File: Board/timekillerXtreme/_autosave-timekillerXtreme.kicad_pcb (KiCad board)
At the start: 2 copper layers, 61.5 x 105.2 mm, 113 parts, among them J1 Battery, J13 CONN_01X03, J16 PE8, J17 PE9, J18 PE10, J19 PD4, J2 USB_OTG, J20 PD1, J21 PD0, J22 PD3, J23 PE11, J24 Pb12, J3 Conn_Bottom_Expansion, J5 Conn_LCD_Board, J6 uSD, J8 TP_AUDIO_R, J9 TP_AUDIO_L, Q1 IRLML6302, Q2 PMBT3904.215, SW1 PWR, SW2 A, SW3 B, SW4 LEFT, SW5 RIGHT, SW6 DOWN, SW7 UP, SW8 RST, U1 MCP73831, U2 FT230XS-R, U3 NCP1529, U4 TLV431, U5 STM32F407VGT6, U6 USBLC6, U7 AOZ1310, U8 USBLC6, U9 USBLC6, Y1 32.768 KHz, Y2 16MHz

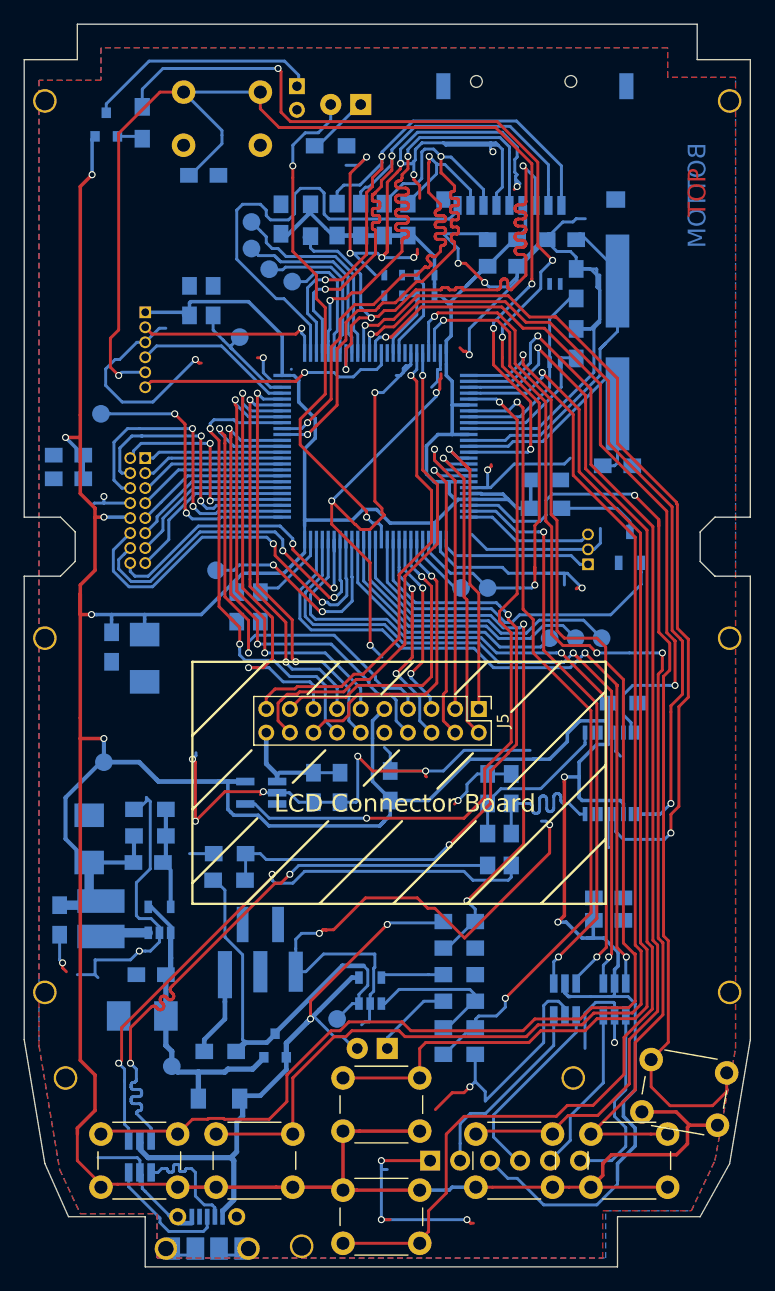
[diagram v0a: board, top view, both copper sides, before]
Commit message: Case and board updated, this will be shipped to the boardhouse and I will call it rev2 if it is ok.
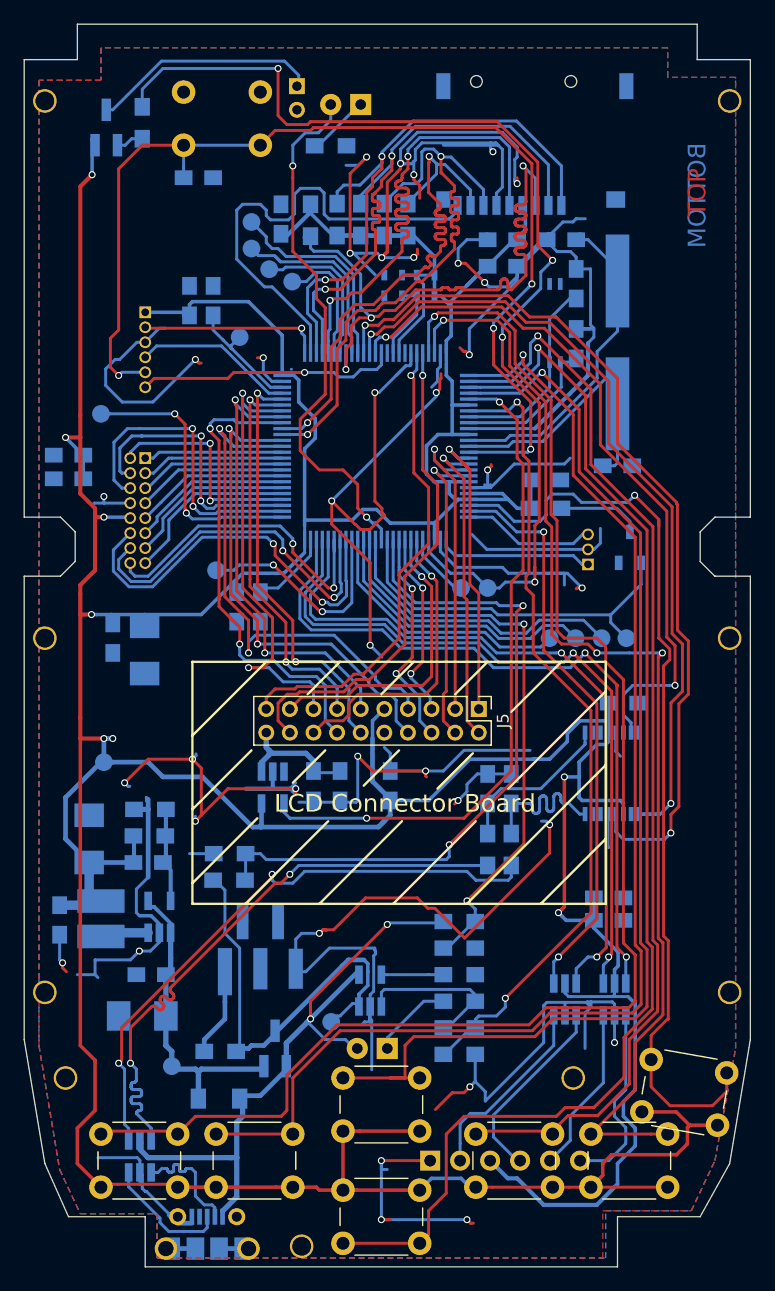
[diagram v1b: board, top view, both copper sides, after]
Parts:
- added VREF: VREF, Measurement_Points:Measurement_Point_Round-SMD-Pad_Small, B.Cu at (168.5, 92.0)
- Q1, Q2: footprint TO_SOT_Packages_SMD:SOT-23 -> TO_SOT_Packages_SMD:SOT-23_Handsoldering
- U1, U3: footprint TO_SOT_Packages_SMD:SOT-23-5 -> TO_SOT_Packages_SMD:SOT-23-5_HandSoldering
- moved SW8 7.91 mm to (137.5, 45.8), turned to 180 degrees
- moved U7 1.07 mm to (138.6, 104.7), turned to 270 degrees
- moved C18 0.76 mm to (125.0, 92.0)
- moved C24 0.70 mm to (127.7, 93.0)
- moved VBATT 0.56 mm to (143.5, 124.5)
- moved C13 0.49 mm to (132.2, 53.0)
- moved U3 0.26 mm to (128.9, 115.6)
- moved J1 0.25 mm to (137.5, 117.8)
- moved Q1 0.25 mm to (138.8, 126.8)
- moved Q2 0.25 mm to (124.5, 48.8)
- moved C32 0.14 mm to (142.0, 104.5)
- moved C33 0.14 mm to (144.2, 104.5)
- moved R8 0.05 mm to (128.1, 108.8)
- renumbered V_USB to VUSB
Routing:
- net RESET: track 105.4 -> 93.7 mm
- net GND: track 475.0 -> 486.5 mm, vias 35 -> 36
- net Net-(C11-Pad1): track 32.2 -> 28.3 mm
- net LCD_BL_SHDN: track 60.3 -> 56.8 mm
- net +3V3: track 503.3 -> 500.2 mm, vias 7 -> 8
- net BTN_1_UP: track 94.3 -> 96.7 mm
- net VBATT_SENSE: track 56.8 -> 59.0 mm
- net BATT+: track 34.9 -> 36.9 mm
- net 1.2VREF: track 29.7 -> 31.7 mm
- net LCD_PWR: track 9.92 -> 11.9 mm
- net BOARD_REV_DETECT1: track 8.95 -> 10.2 mm
- net USB_VBUS: track 57.7 -> 58.9 mm
- net SYS_LED: track 44.0 -> 45.0 mm
- net Net-(C3-Pad1): track 23.9 -> 24.6 mm
- net EXC2_10: track 23.8 -> 23.2 mm
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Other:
- board text added: "Rev. 2 2018-11-14"
- board text added: "solder flat"
- board text removed: "Rev. 2 2018-11-04"
